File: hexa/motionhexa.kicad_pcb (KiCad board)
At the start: 4 copper layers, 78 x 67.5 mm, 298 parts, among them J1 Conn_01x06_Socket, Q1 Q_Photo_NPN

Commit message: layout improvements; silkscreen
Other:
- board text added: "PS+"
- board text added: "PSR"
- board text removed: "PHOTO"
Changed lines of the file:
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@@
 		)
 	)
-	(gr_text "PHOTO"
-		(at 115.062 67.7672 150)
+	(gr_text "PS+"
+		(at 114.3 67.2846 150)
 		(layer "B.SilkS")
 		(effects
@@
 		(layer "B.SilkS")
 		(effects
+			(font
+				(size 1.2 1.2)
+				(thickness 0.15)
+			)
+			(justify left bottom mirror)
+		)
+	)
+	(gr_text "PSR"
+		(at 117.9322 69.3674 150)
+		(layer "B.SilkS")
+		(effects

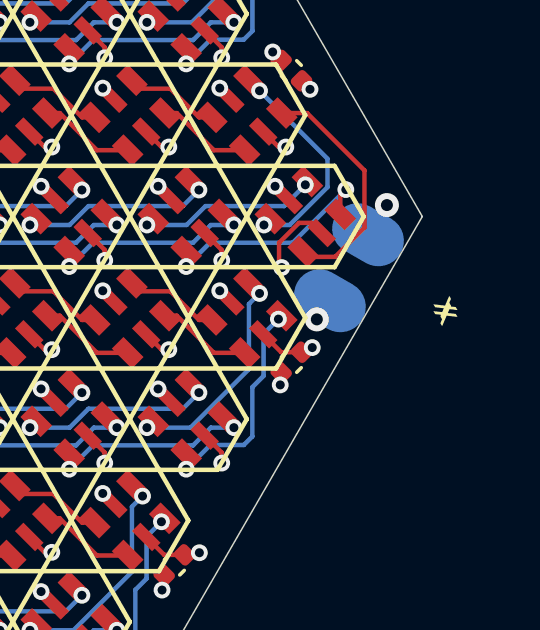
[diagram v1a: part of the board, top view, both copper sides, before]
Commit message: remove stray silk
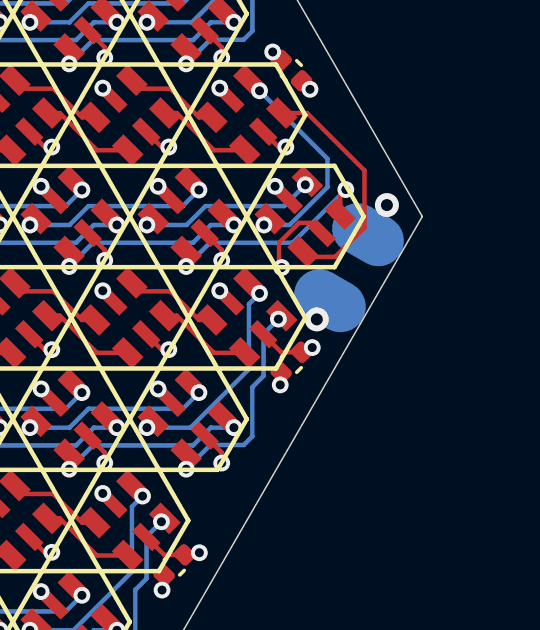
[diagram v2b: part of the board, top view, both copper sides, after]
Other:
- board text removed: "x"
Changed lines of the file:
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@@
-		)
-	)
-	(gr_text "x"
-		(at 139.2682 102.9462 300)
-		(layer "F.SilkS")
-		(effects
-			(font
-				(size 0.8 0.8)
-				(thickness 0.12)
-			)
-			(justify left bottom)
-		)
-	)
-	(gr_text "x"
-		(at 139.2682 103.1748 300)
-		(layer "F.SilkS")
-		(effects
-			(font
-				(size 0.8 0.8)
-				(thickness 0.12)
-			)
-			(justify left bottom)
 		)
 	)
